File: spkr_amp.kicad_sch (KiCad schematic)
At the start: 2 parts, among them U3 TPA2006D1DRBR

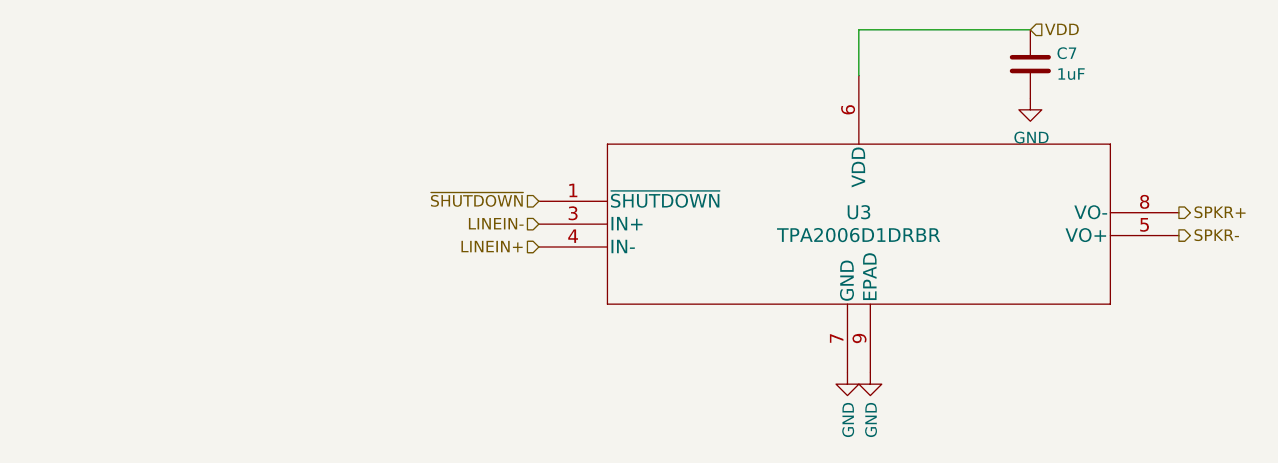
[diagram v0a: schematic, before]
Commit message: Schematic: switch to AIC3206 to get ground-centered headphone outputs, and just wire up directly to a raspberry pi 40-pin header instead of using 1mm headers.
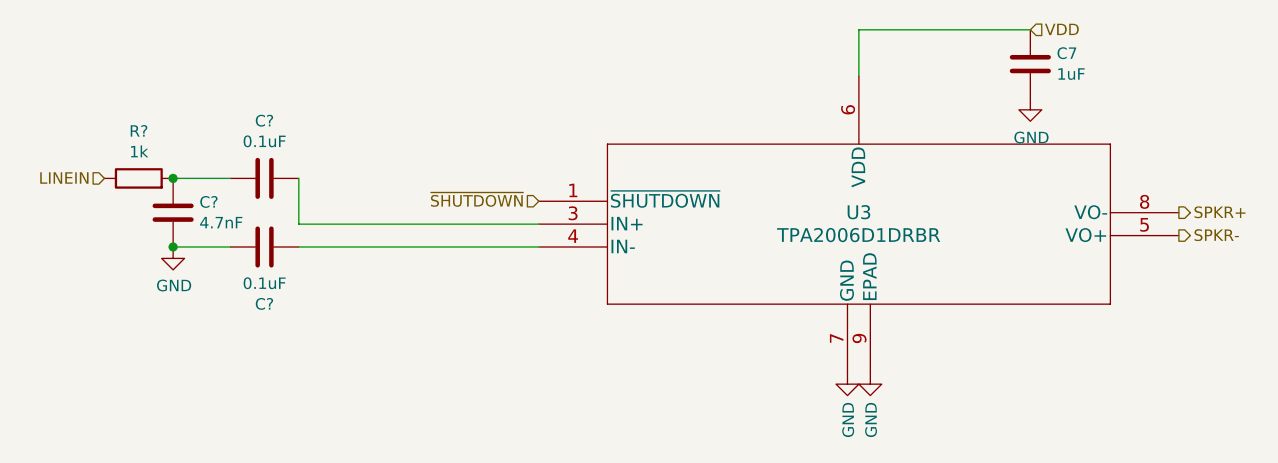
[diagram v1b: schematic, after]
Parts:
- added C? (x2): 0.1uF, symbol Device:C
- added C?: 4.7nF, symbol Device:C
- added R?: 1k, symbol Device:R
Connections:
- net GND: now also C?.1, C?.2
- net LINEIN+: no longer names the net of U3.4 (IN-)
- net LINEIN+: now also C?.2
- net LINEIN-: no longer names the net of U3.3 (IN+)
- net LINEIN-: now also C?.2
- new net: C?.1, C?.1, R?.2
- new net LINEIN: R?.1
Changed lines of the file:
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@@
 (kicad_sch (version 20210126) (generator eeschema)
   (paper "A4")
+  (junction (at 95.25 78.74) (diameter 1.016) (color 0 0 0 0))
+  (junction (at 95.25 86.36) (diameter 1.016) (color 0 0 0 0))
+  (wire (pts (xy 95.25 78.74) (xy 101.6 78.74))
+    (stroke (width 0) (type solid) (color 0 0 0 0))
+  )
+  (wire (pts (xy 95.25 86.36) (xy 101.6 86.36))
+    (stroke (width 0) (type solid) (color 0 0 0 0))
+  )
+  (wire (pts (xy 109.22 83.82) (xy 109.22 78.74))
+    (stroke (width 0) (type solid) (color 0 0 0 0))
+  )
+  (wire (pts (xy 109.22 86.36) (xy 135.89 86.36))
+    (stroke (width 0) (type solid) (color 0 0 0 0))
+  )
+  (wire (pts (xy 135.89 83.82) (xy 109.22 83.82))
+    (stroke (width 0) (type solid) (color 0 0 0 0))
+  )
   (wire (pts (xy 171.45 62.23) (xy 171.45 67.31))
     (stroke (width 0) (type solid) (color 0 0 0 0))
@@
     (stroke (width 0) (type solid) (color 0 0 0 0))
   )
-  (hierarchical_label "~SHUTDOWN" (shape input) (at 135.89 81.28 180)
+  (hierarchical_label "LINEIN" (shape input) (at 87.63 78.74 180)
     (effects (font (size 1.27 1.27)) (justify right))
   )
-  (hierarchical_label "LINEIN-" (shape input) (at 135.89 83.82 180)
-    (effects (font (size 1.27 1.27)) (justify right))
-  )
-  (hierarchical_label "LINEIN+" (shape input) (at 135.89 86.36 180)
+  (hierarchical_label "~SHUTDOWN" (shape input) (at 135.89 81.28 180)
     (effects (font (size 1.27 1.27)) (justify right))
   )
@@
   (hierarchical_label "SPKR-" (shape output) (at 207.01 85.09 0)
     (effects (font (size 1.27 1.27)) (justify left))
+  )
+  (symbol (lib_id "power:GND") (at 95.25 86.36 0)
+    (in_bom yes) (on_board yes)
+    (property "Reference" "#PWR?" (id 0) (at 95.25 92.71 0)
+      (effects (font (size 1.27 1.27)) hide)
+    )
+    (property "Value" "GND" (id 1) (at 95.3643 90.6844 0))
+    (property "Footprint" "" (id 2) (at 95.25 86.36 0)
+      (effects (font (size 1.27 1.27)) hide)
+    )
+    (property "Datasheet" "" (id 3) (at 95.25 86.36 0)
+      (effects (font (size 1.27 1.27)) hide)
+    )
+    (pin "1")
   )
   (symbol (lib_id "power:GND") (at 170.18 100.33 0)
@@
     (pin "1")
   )
+  (symbol (lib_id "Device:R") (at 91.44 78.74 90)
+    (in_bom yes) (on_board yes)
+    (property "Reference" "R?" (id 0) (at 91.44 73.5138 90))
+    (property "Value" "1k" (id 1) (at 91.44 75.812 90))
+    (property "Footprint" "" (id 2) (at 91.44 80.518 90)
+      (effects (font (size 1.27 1.27)) hide)
+    )
+    (property "Datasheet" "~" (id 3) (at 91.44 78.74 0)
+      (effects (font (size 1.27 1.27)) hide)
+    )
+    (pin "1")
+    (pin "2")
+  )
+  (symbol (lib_id "Device:C") (at 95.25 82.55 0)
+    (in_bom yes) (on_board yes)
+    (property "Reference" "C?" (id 0) (at 98.1711 81.4006 0)
+      (effects (font (size 1.27 1.27)) (justify left))
+    )
+    (property "Value" "4.7nF" (id 1) (at 98.171 83.699 0)
+      (effects (font (size 1.27 1.27)) (justify left))
+    )
+    (property "Footprint" "" (id 2) (at 96.2152 86.36 0)
+      (effects (font (size 1.27 1.27)) hide)
+    )
+    (property "Datasheet" "~" (id 3) (at 95.25 82.55 0)
+      (effects (font (size 1.27 1.27)) hide)
+    )
+    (pin "1")
+    (pin "2")
+  )
+  (symbol (lib_id "Device:C") (at 105.41 78.74 90)
+    (in_bom yes) (on_board yes)
+    (property "Reference" "C?" (id 0) (at 105.41 72.3708 90))
+    (property "Value" "0.1uF" (id 1) (at 105.41 74.669 90))
+    (property "Footprint" "" (id 2) (at 109.22 77.7748 0)
+      (effects (font (size 1.27 1.27)) hide)
+    )
+    (property "Datasheet" "~" (id 3) (at 105.41 78.74 0)
+      (effects (font (size 1.27 1.27)) hide)
+    )
+    (pin "1")
+    (pin "2")
+  )
+  (symbol (lib_id "Device:C") (at 105.41 86.36 90)
+    (in_bom yes) (on_board yes)
+    (property "Reference" "C?" (id 0) (at 105.41 92.7292 90))
+    (property "Value" "0.1uF" (id 1) (at 105.41 90.43 90))
+    (property "Footprint" "" (id 2) (at 109.22 85.3948 0)
+      (effects (font (size 1.27 1.27)) hide)
+    )
+    (property "Datasheet" "~" (id 3) (at 105.41 86.36 0)
+      (effects (font (size 1.27 1.27)) hide)
+    )
+    (pin "1")
+    (pin "2")
+  )
   (symbol (lib_id "Device:C") (at 190.5 66.04 0)

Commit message: lay out new version with AIC3206 codec
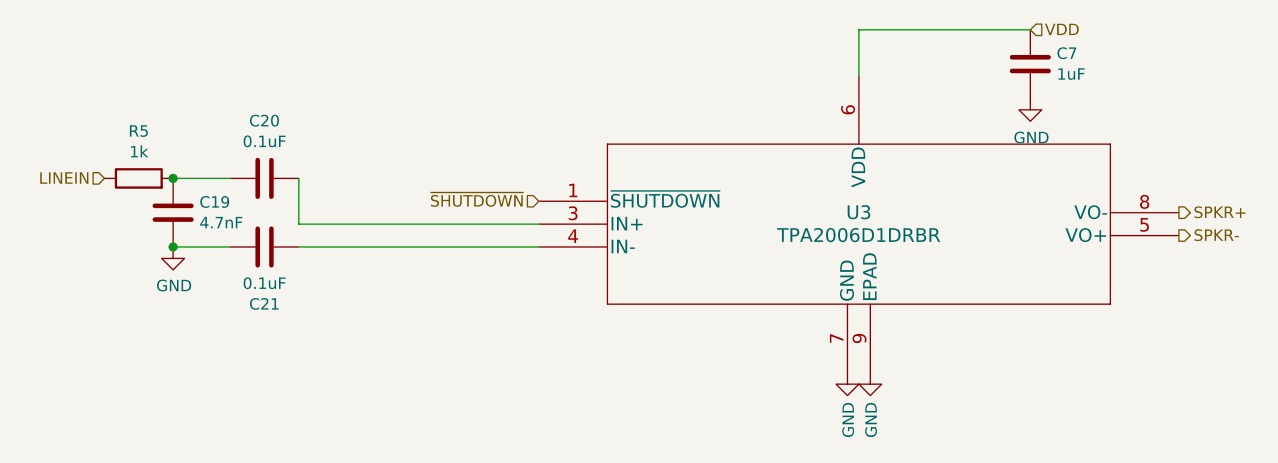
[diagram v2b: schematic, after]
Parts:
- C19, C20, C21: renamed from C?; footprint (none) -> Capacitor_SMD:C_0402_1005Metric
- R5: renamed from R?; footprint (none) -> Resistor_SMD:R_0402_1005Metric
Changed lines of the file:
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@@
   (symbol (lib_id "power:GND") (at 95.25 86.36 0)
     (in_bom yes) (on_board yes)
-    (property "Reference" "#PWR?" (id 0) (at 95.25 92.71 0)
+    (property "Reference" "#PWR019" (id 0) (at 95.25 92.71 0)
       (effects (font (size 1.27 1.27)) hide)
     )
@@
   (symbol (lib_id "Device:R") (at 91.44 78.74 90)
     (in_bom yes) (on_board yes)
-    (property "Reference" "R?" (id 0) (at 91.44 73.5138 90))
+    (property "Reference" "R5" (id 0) (at 91.44 73.5138 90))
     (property "Value" "1k" (id 1) (at 91.44 75.812 90))
-    (property "Footprint" "" (id 2) (at 91.44 80.518 90)
+    (property "Footprint" "Resistor_SMD:R_0402_1005Metric" (id 2) (at 91.44 80.518 90)
       (effects (font (size 1.27 1.27)) hide)
     )
@@
   (symbol (lib_id "Device:C") (at 95.25 82.55 0)
     (in_bom yes) (on_board yes)
-    (property "Reference" "C?" (id 0) (at 98.1711 81.4006 0)
+    (property "Reference" "C19" (id 0) (at 98.1711 81.4006 0)
       (effects (font (size 1.27 1.27)) (justify left))
     )
@@
       (effects (font (size 1.27 1.27)) (justify left))
     )
-    (property "Footprint" "" (id 2) (at 96.2152 86.36 0)
+    (property "Footprint" "Capacitor_SMD:C_0402_1005Metric" (id 2) (at 96.2152 86.36 0)
       (effects (font (size 1.27 1.27)) hide)
     )
@@
   (symbol (lib_id "Device:C") (at 105.41 78.74 90)
     (in_bom yes) (on_board yes)
-    (property "Reference" "C?" (id 0) (at 105.41 72.3708 90))
+    (property "Reference" "C20" (id 0) (at 105.41 72.3708 90))
     (property "Value" "0.1uF" (id 1) (at 105.41 74.669 90))
-    (property "Footprint" "" (id 2) (at 109.22 77.7748 0)
+    (property "Footprint" "Capacitor_SMD:C_0402_1005Metric" (id 2) (at 109.22 77.7748 0)
       (effects (font (size 1.27 1.27)) hide)
     )
@@
   (symbol (lib_id "Device:C") (at 105.41 86.36 90)
     (in_bom yes) (on_board yes)
-    (property "Reference" "C?" (id 0) (at 105.41 92.7292 90))
+    (property "Reference" "C21" (id 0) (at 105.41 92.7292 90))
     (property "Value" "0.1uF" (id 1) (at 105.41 90.43 90))
-    (property "Footprint" "" (id 2) (at 109.22 85.3948 0)
+    (property "Footprint" "Capacitor_SMD:C_0402_1005Metric" (id 2) (at 109.22 85.3948 0)
       (effects (font (size 1.27 1.27)) hide)
     )

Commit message: Refactor everything but headers into a hierarchical sheet.
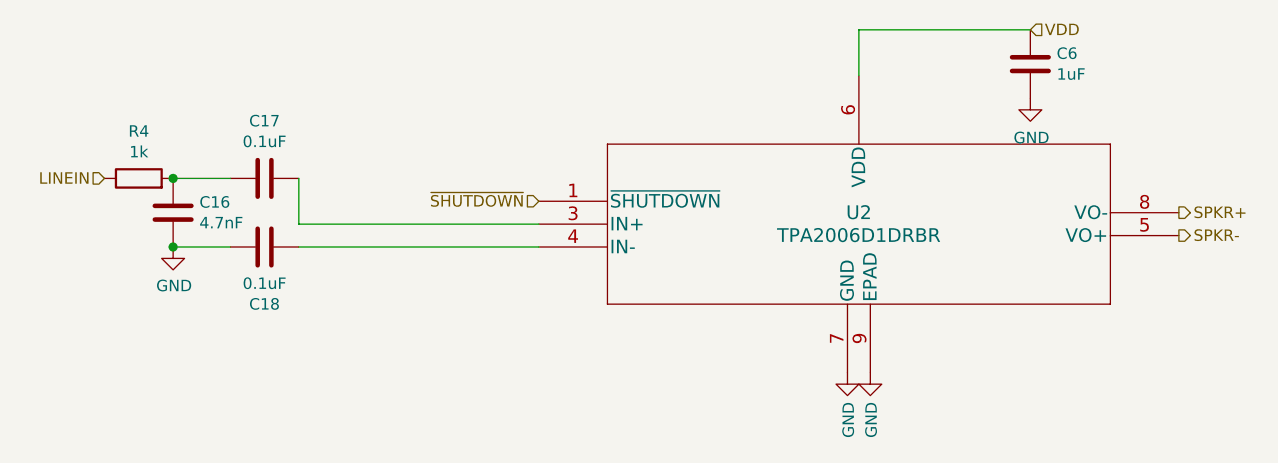
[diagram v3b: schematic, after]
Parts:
- renumbered C19 to C16, C20 to C17, C21 to C18, C7 to C6, R5 to R4, U3 to U2
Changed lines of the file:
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@@
   (symbol (lib_id "power:GND") (at 95.25 86.36 0)
     (in_bom yes) (on_board yes)
-    (property "Reference" "#PWR019" (id 0) (at 95.25 92.71 0)
+    (property "Reference" "#PWR0112" (id 0) (at 95.25 92.71 0)
       (effects (font (size 1.27 1.27)) hide)
     )
@@
   (symbol (lib_id "power:GND") (at 170.18 100.33 0)
     (in_bom yes) (on_board yes)
-    (property "Reference" "#PWR08" (id 0) (at 170.18 106.68 0)
+    (property "Reference" "#PWR0116" (id 0) (at 170.18 106.68 0)
       (effects (font (size 1.27 1.27)) hide)
     )
@@
   (symbol (lib_id "power:GND") (at 172.72 100.33 0)
     (in_bom yes) (on_board yes)
-    (property "Reference" "#PWR09" (id 0) (at 172.72 106.68 0)
+    (property "Reference" "#PWR0117" (id 0) (at 172.72 106.68 0)
       (effects (font (size 1.27 1.27)) hide)
     )
@@
   (symbol (lib_id "power:GND") (at 190.5 69.85 0)
     (in_bom yes) (on_board yes)
-    (property "Reference" "#PWR010" (id 0) (at 190.5 76.2 0)
+    (property "Reference" "#PWR0118" (id 0) (at 190.5 76.2 0)
       (effects (font (size 1.27 1.27)) hide)
     )
@@
   (symbol (lib_id "Device:R") (at 91.44 78.74 90)
     (in_bom yes) (on_board yes)
-    (property "Reference" "R5" (id 0) (at 91.44 73.5138 90))
+    (property "Reference" "R4" (id 0) (at 91.44 73.5138 90))
     (property "Value" "1k" (id 1) (at 91.44 75.812 90))
     (property "Footprint" "Resistor_SMD:R_0402_1005Metric" (id 2) (at 91.44 80.518 90)
@@
   (symbol (lib_id "Device:C") (at 95.25 82.55 0)
     (in_bom yes) (on_board yes)
-    (property "Reference" "C19" (id 0) (at 98.1711 81.4006 0)
+    (property "Reference" "C16" (id 0) (at 98.1711 81.4006 0)
       (effects (font (size 1.27 1.27)) (justify left))
     )
@@
   (symbol (lib_id "Device:C") (at 105.41 78.74 90)
     (in_bom yes) (on_board yes)
-    (property "Reference" "C20" (id 0) (at 105.41 72.3708 90))
+    (property "Reference" "C17" (id 0) (at 105.41 72.3708 90))
     (property "Value" "0.1uF" (id 1) (at 105.41 74.669 90))
     (property "Footprint" "Capacitor_SMD:C_0402_1005Metric" (id 2) (at 109.22 77.7748 0)
@@
   (symbol (lib_id "Device:C") (at 105.41 86.36 90)
     (in_bom yes) (on_board yes)
-    (property "Reference" "C21" (id 0) (at 105.41 92.7292 90))
+    (property "Reference" "C18" (id 0) (at 105.41 92.7292 90))
     (property "Value" "0.1uF" (id 1) (at 105.41 90.43 90))
     (property "Footprint" "Capacitor_SMD:C_0402_1005Metric" (id 2) (at 109.22 85.3948 0)
@@
   (symbol (lib_id "Device:C") (at 190.5 66.04 0)
     (in_bom yes) (on_board yes)
-    (property "Reference" "C7" (id 0) (at 193.421 64.8716 0)
+    (property "Reference" "C6" (id 0) (at 193.421 64.8716 0)
       (effects (font (size 1.27 1.27)) (justify left))
     )
@@
   (symbol (lib_id "TPA2006D1DRBR:TPA2006D1DRBR") (at 171.45 83.82 0)
     (in_bom yes) (on_board yes)
-    (property "Reference" "U3" (id 0) (at 171.45 82.55 0)
+    (property "Reference" "U2" (id 0) (at 171.45 82.55 0)
       (effects (font (size 1.524 1.524)))
     )

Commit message: Route CM4 board with differential connector on the right.
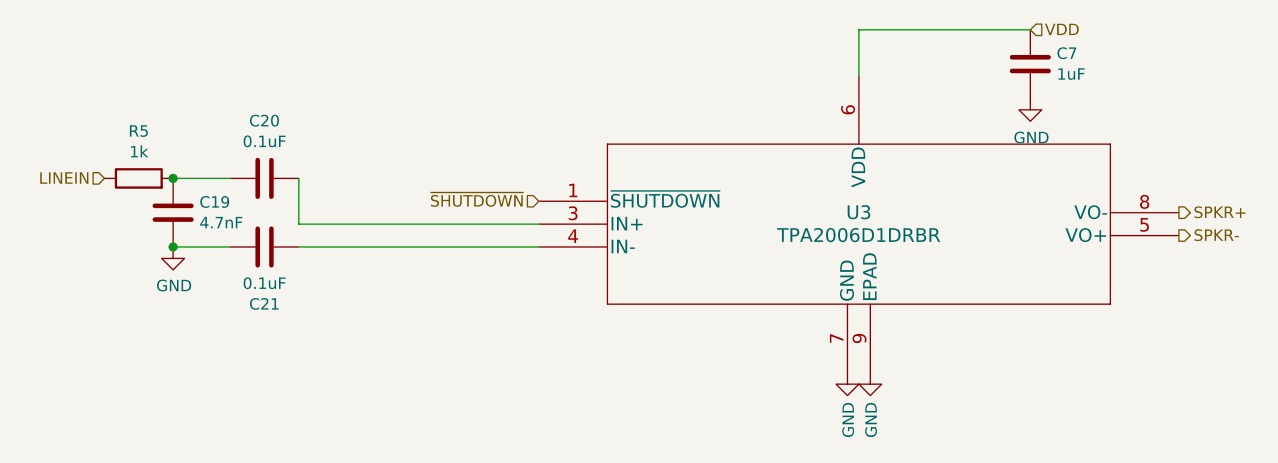
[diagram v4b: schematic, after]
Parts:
- renumbered C16 to C19, C17 to C20, C18 to C21, C6 to C7, R4 to R5, U2 to U3
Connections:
- net ~SHUTDOWN renamed ~{SHUTDOWN}

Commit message: Switch tps61176 for tps61177, since 61176 is out of stock. Also finish fixing hole clearance violations.
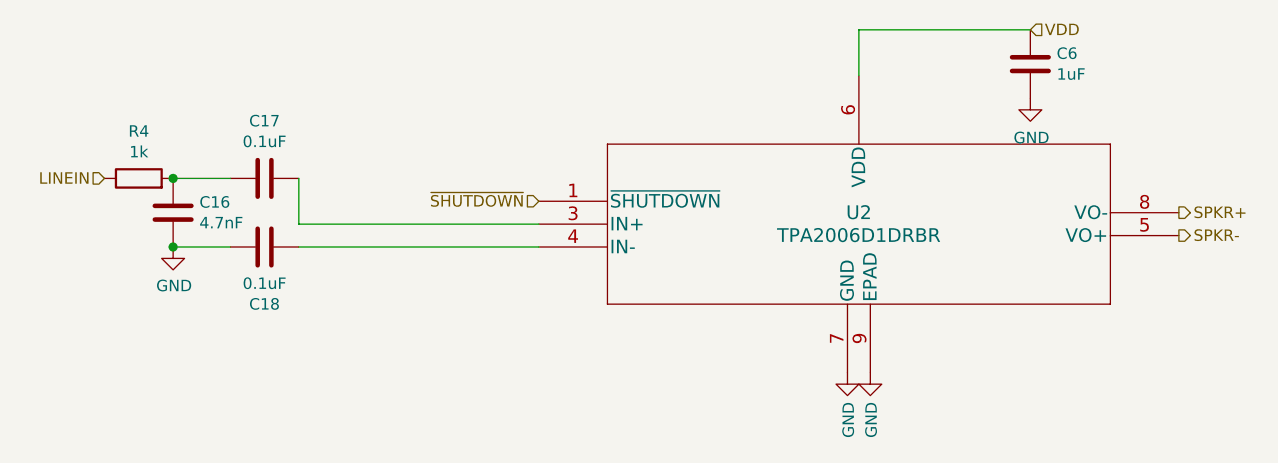
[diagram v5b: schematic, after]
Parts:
- renumbered C19 to C16, C20 to C17, C21 to C18, C7 to C6, R5 to R4, U3 to U2
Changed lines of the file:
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@@
   (symbol (lib_id "Device:C") (at 190.5 66.04 0)
     (in_bom yes) (on_board yes)
-    (property "Reference" "C7" (id 0) (at 193.421 64.8716 0)
+    (property "Reference" "C6" (id 0) (at 193.421 64.8716 0)
       (effects (font (size 1.27 1.27)) (justify left))
     )
@@
   (symbol (lib_id "TPA2006D1DRBR:TPA2006D1DRBR") (at 171.45 83.82 0)
     (in_bom yes) (on_board yes)
-    (property "Reference" "U3" (id 0) (at 171.45 82.55 0)
+    (property "Reference" "U2" (id 0) (at 171.45 82.55 0)
       (effects (font (size 1.524 1.524)))
     )
@@
   (symbol (lib_id "Device:C") (at 105.41 78.74 90)
     (in_bom yes) (on_board yes)
-    (property "Reference" "C20" (id 0) (at 105.41 72.3708 90))
+    (property "Reference" "C17" (id 0) (at 105.41 72.3708 90))
     (property "Value" "0.1uF" (id 1) (at 105.41 74.669 90))
     (property "Footprint" "Capacitor_SMD:C_0402_1005Metric" (id 2) (at 109.22 77.7748 0)
@@
   (symbol (lib_id "Device:R") (at 91.44 78.74 90)
     (in_bom yes) (on_board yes)
-    (property "Reference" "R5" (id 0) (at 91.44 73.5138 90))
+    (property "Reference" "R4" (id 0) (at 91.44 73.5138 90))
     (property "Value" "1k" (id 1) (at 91.44 75.812 90))
     (property "Footprint" "Resistor_SMD:R_0402_1005Metric" (id 2) (at 91.44 80.518 90)
@@
   (symbol (lib_id "Device:C") (at 105.41 86.36 90)
     (in_bom yes) (on_board yes)
-    (property "Reference" "C21" (id 0) (at 105.41 92.7292 90))
+    (property "Reference" "C18" (id 0) (at 105.41 92.7292 90))
     (property "Value" "0.1uF" (id 1) (at 105.41 90.43 90))
     (property "Footprint" "Capacitor_SMD:C_0402_1005Metric" (id 2) (at 109.22 85.3948 0)
@@
   (symbol (lib_id "Device:C") (at 95.25 82.55 0)
     (in_bom yes) (on_board yes)
-    (property "Reference" "C19" (id 0) (at 98.1711 81.4006 0)
+    (property "Reference" "C16" (id 0) (at 98.1711 81.4006 0)
       (effects (font (size 1.27 1.27)) (justify left))
     )
